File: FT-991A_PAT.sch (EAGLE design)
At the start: 24 parts, among them Q1 J310, Q2 BFS17

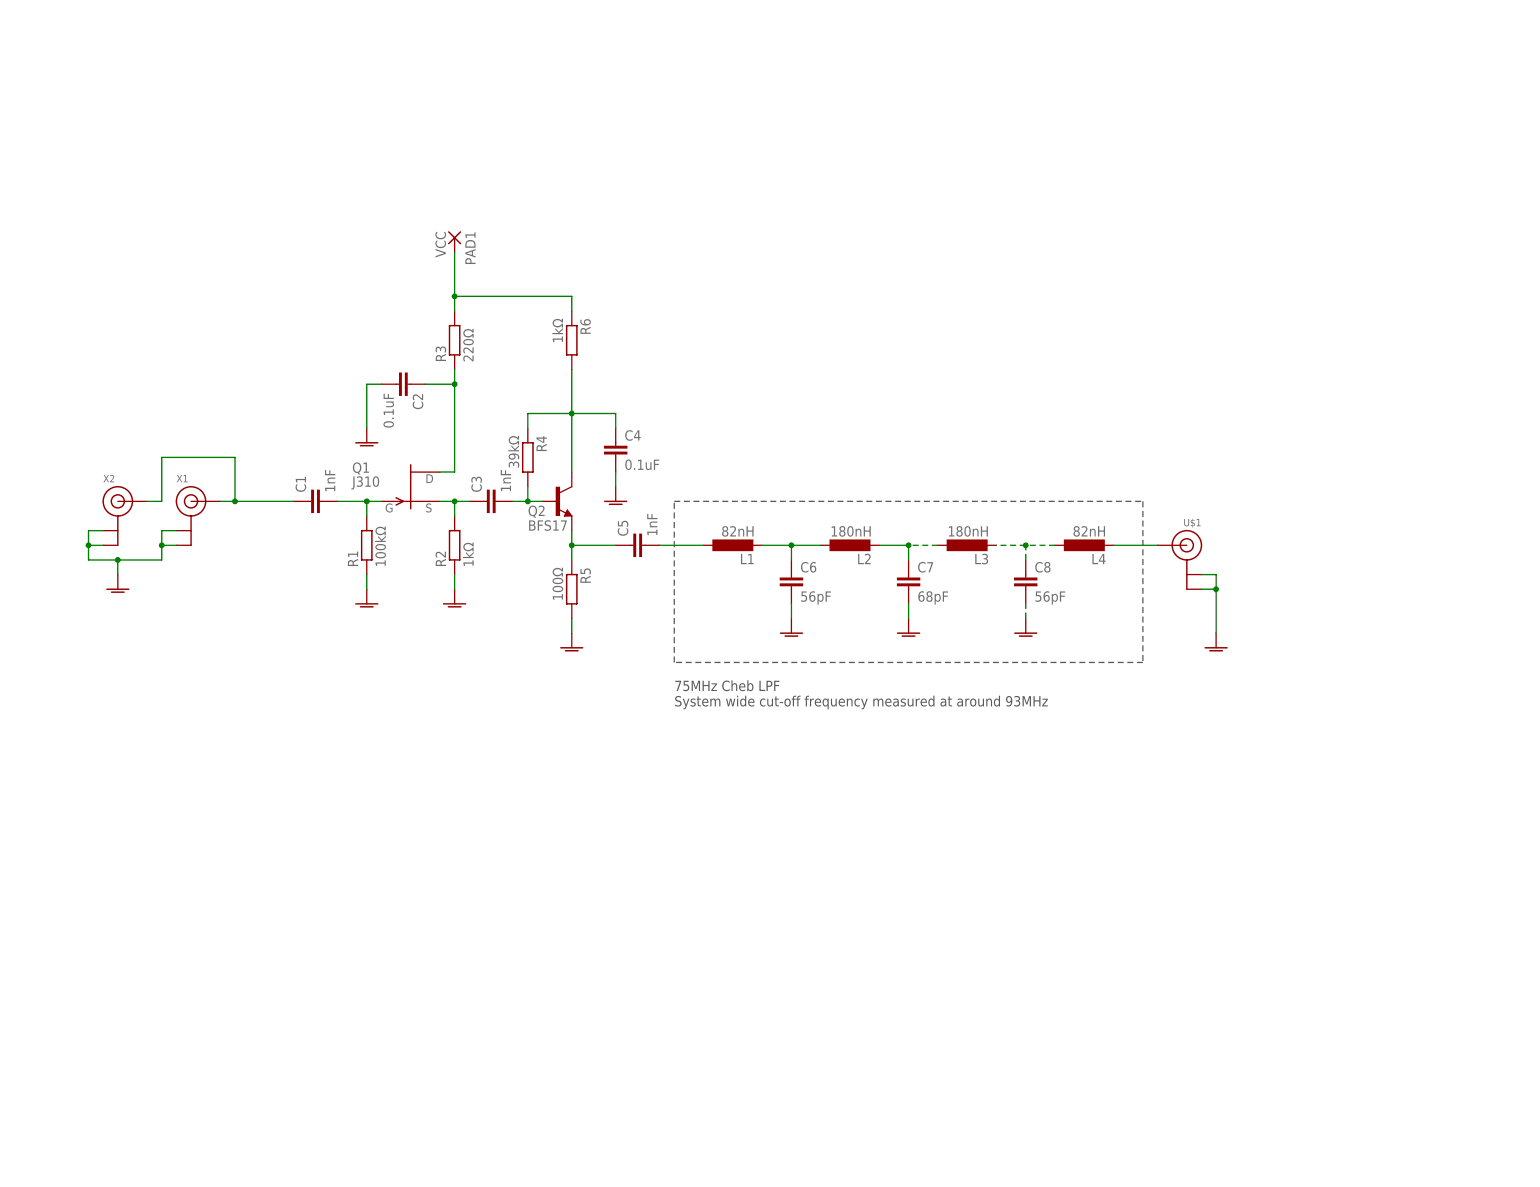
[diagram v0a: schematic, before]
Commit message: Revision D
- Reusing OE2DOR design
- Added a AND gate and a switch to be able to control the IF traffic
to the dongle
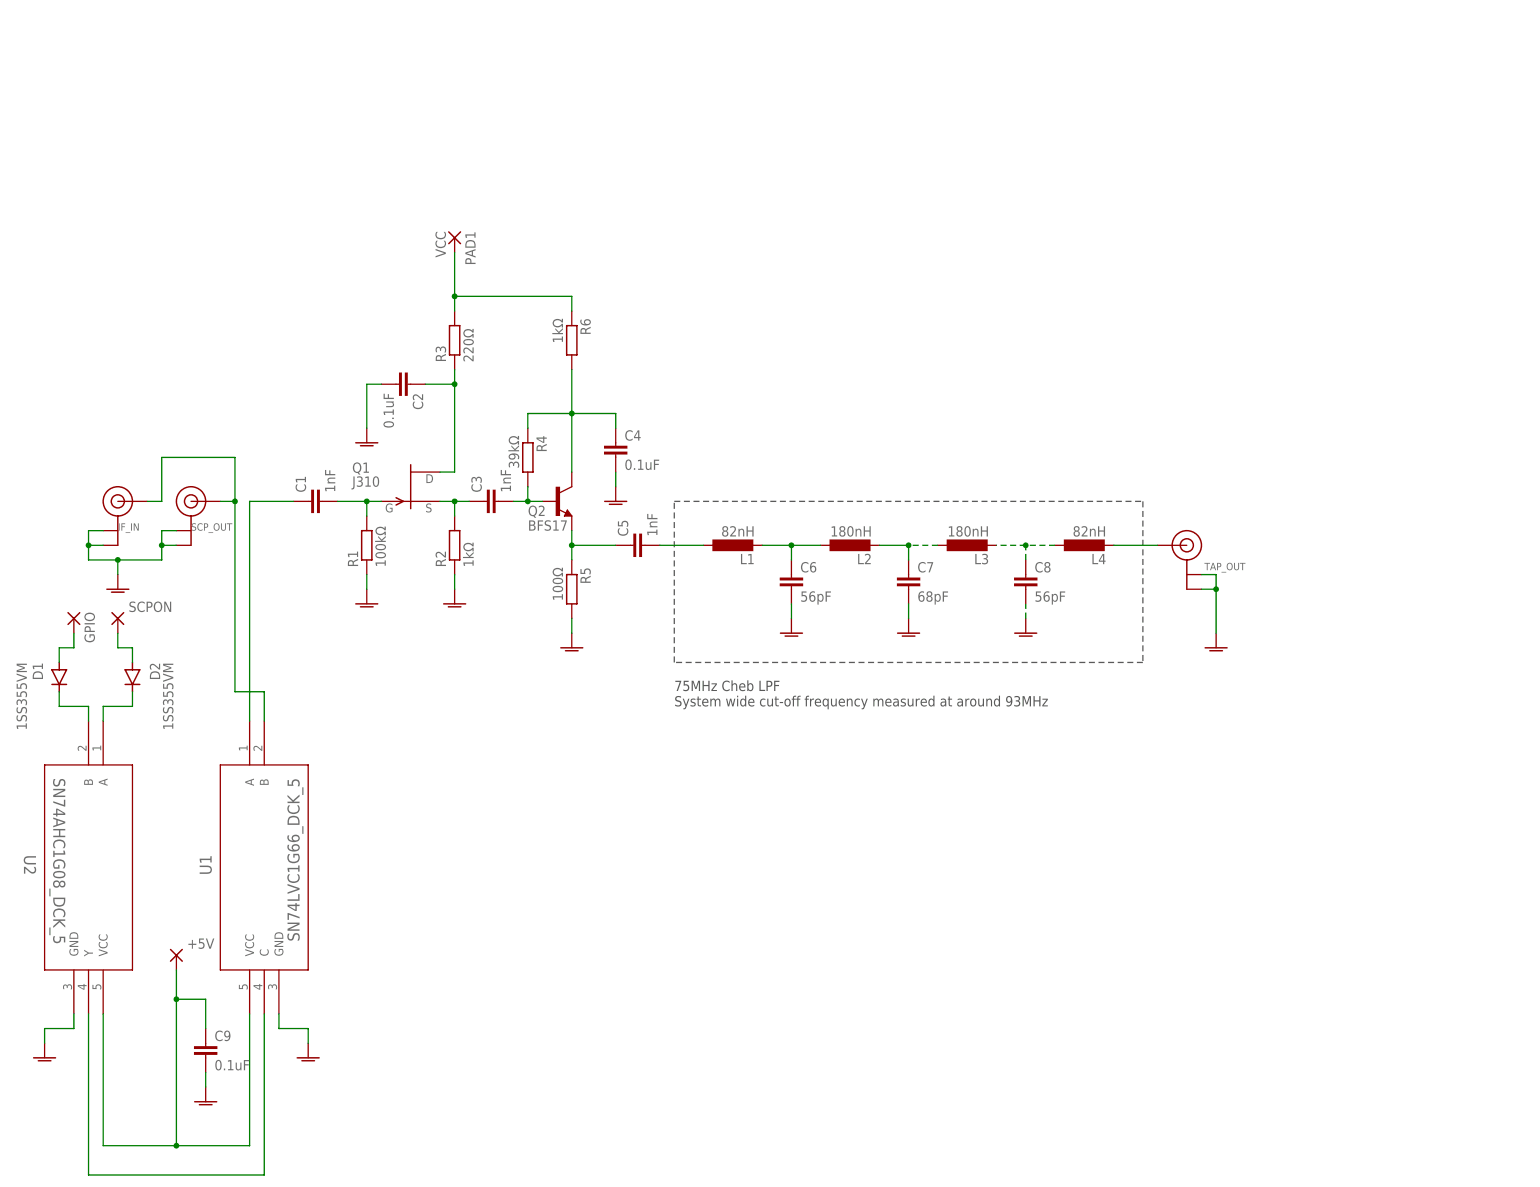
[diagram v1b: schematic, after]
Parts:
- added +5V, GPIO, SCPON: WIREPADSMD1,27-254, wirepad:WIREPADSMD1,27-254
- added C9: 0.1uF, rcl:C-EUC0805K
- added D1, D2: 1SS355VM, diode:DIODE-SOD323-W
- added U1: SN74LVC1G66_DCK_5, sn74lvc1g66-dck:SN74LVC1G66_DCK_5
- added U2: SN74AHC1G08_DCK_5, sn74ahc1g08-dck:SN74AHC1G08_DCK_5
- TAP_OUT: value (none) -> TAP_OUT
- X1: value (none) -> SCP_OUT
- X2: value (none) -> IF_IN
- renumbered U$1 to TAP_OUT
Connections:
- new net N$16: D1.A, GPIO.P
- new net N$17: D1.C, U2.B
- new net N$18: D2.A, SCPON.P
- new net N$20: D2.C, U2.A
- new net N$22: U1.C, U2.Y
- new net N$7: U1.B, X1.SIGNAL, X2.SIGNAL
- new net VCC: +5V.P, C9.1, U1.VCC, U2.VCC
- net GNDA: now also C9.2, U1.GND, U2.GND
- net N$14: now also U1.A; no longer X1.SIGNAL, X2.SIGNAL

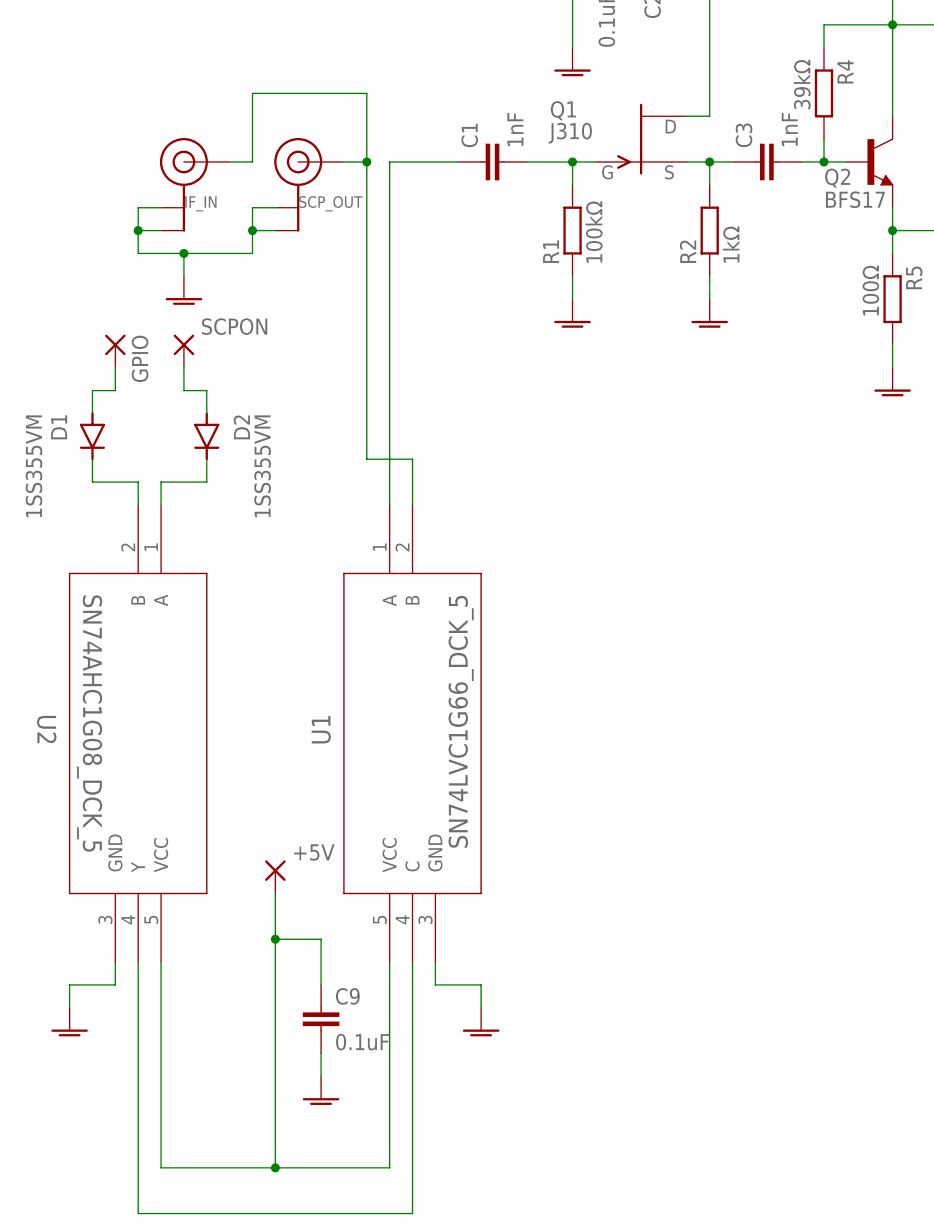
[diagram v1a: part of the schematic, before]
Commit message: Revision E
 - Now sports a RF switch (PE4259) instead of a regular Analog switch
   (was: SN74LVC1G66);
   * Also contains its resistors as per reference design;
- Changed voltage from 5V to 3.3V to Switch and AND port;
- SDR output will be grounded by default when switch is in default state
  (RF 2 port) port
- Updated list of contributors in Silk Screen.
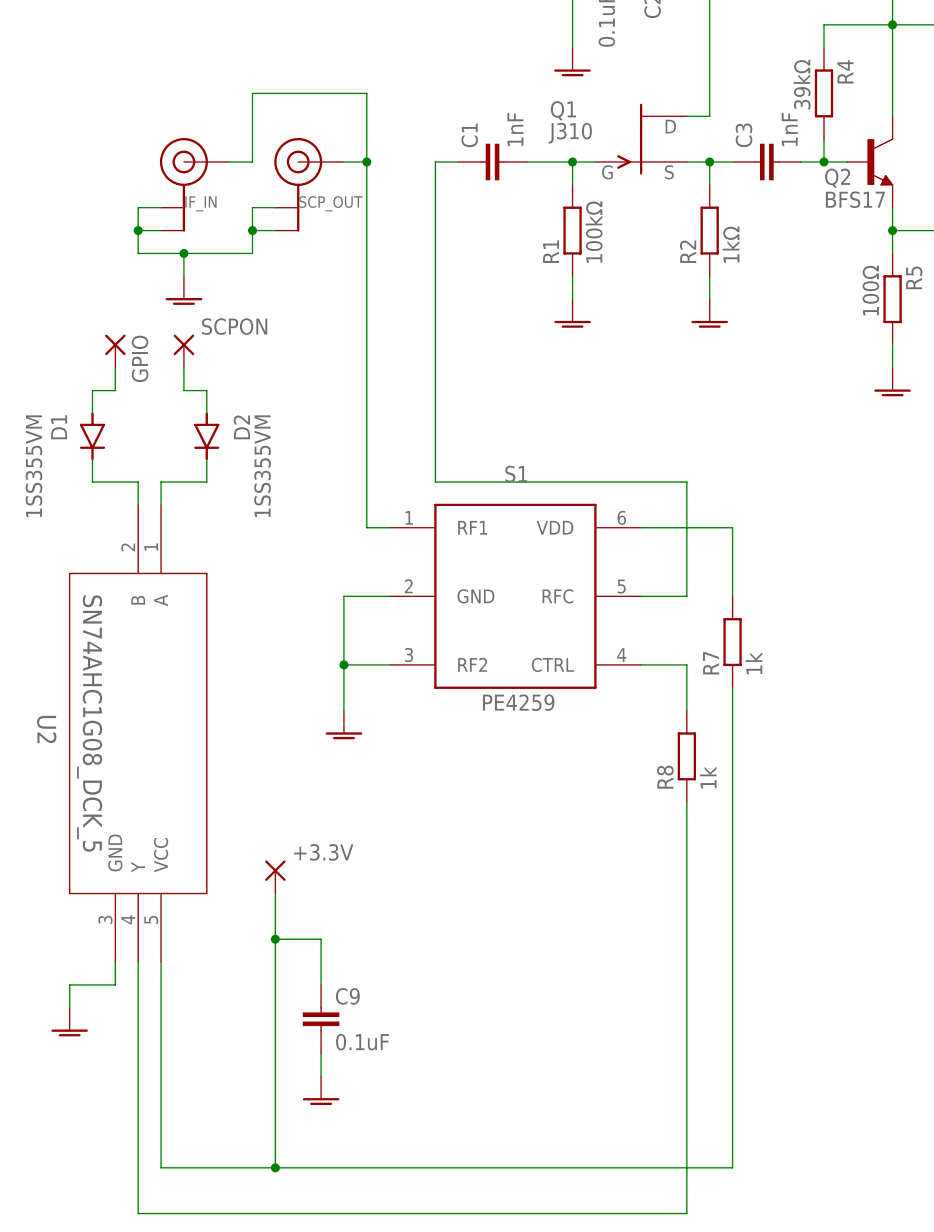
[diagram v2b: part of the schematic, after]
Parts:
- removed U1: SN74LVC1G66_DCK_5, sn74lvc1g66-dck:SN74LVC1G66_DCK_5
- added R7, R8: 1k, rcl:R-EU_R0805
- added S1: PE4259, psemi:PE4259
- renumbered +5V to +3.3V
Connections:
- removed net N$14: C1.1, U1.A
- new net N$15: C1.1, S1.RFC
- new net N$19: R8.2, S1.CTRL
- new net VDD: R7.2, S1.VDD
- net GNDA: now also S1.GND, S1.RF2; no longer U1.GND
- net N$22: now also R8.1; no longer U1.C
- net N$7: now also S1.RF1; no longer U1.B
- net VCC: now also R7.1; no longer U1.VCC
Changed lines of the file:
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@@
 <attribute name="PROJECT_INFO" value="Yaesu FT-991A Panadapter with Signal Control"/>
 <attribute name="PROJECT_NAME" value="FT-991A PAT &amp; SDR"/>
-<attribute name="REVISION_ID" value="D"/>
+<attribute name="REVISION_ID" value="E"/>
 </attributes>
 <variantdefs>
@@
 <part name="X2" library="adafruit" deviceset="ANTENNA_U.FL" device="" value="IF_IN"/>
 <part name="GND11" library="supply1" deviceset="GNDA" device=""/>
-<part name="U1" library="sn74lvc1g66-dck" deviceset="SN74LVC1G66_DCK_5" device=""/>
 <part name="U2" library="sn74ahc1g08-dck" deviceset="SN74AHC1G08_DCK_5" device=""/>
 <part name="D1" library="diode" library_urn="urn:adsk.eagle:library:210" deviceset="DIODE-" device="SOD323-W" package3d_urn="urn:adsk.eagle:package:43418/1" value="1SS355VM"/>
@@
 <part name="GPIO" library="wirepad" library_urn="urn:adsk.eagle:library:412" deviceset="WIREPAD" device="SMD1,27-254" package3d_urn="urn:adsk.eagle:package:30839/1" value=""/>
 <part name="SCPON" library="wirepad" library_urn="urn:adsk.eagle:library:412" deviceset="WIREPAD" device="SMD1,27-254" package3d_urn="urn:adsk.eagle:package:30839/1" value=""/>
-<part name="+5V" library="wirepad" library_urn="urn:adsk.eagle:library:412" deviceset="WIREPAD" device="SMD1,27-254" package3d_urn="urn:adsk.eagle:package:30839/1" value=""/>
+<part name="+3.3V" library="wirepad" library_urn="urn:adsk.eagle:library:412" deviceset="WIREPAD" device="SMD1,27-254" package3d_urn="urn:adsk.eagle:package:30839/1" value=""/>
+<part name="S1" library="psemi" deviceset="PE4259" device="" value="PE4259"/>
+<part name="R7" library="rcl" deviceset="R-EU_" device="R0805" value="1k"/>
+<part name="R8" library="rcl" deviceset="R-EU_" device="R0805" value="1k"/>
 </parts>
 <sheets>
@@
 </instance>
 <instance part="GND11" gate="1" x="78.74" y="114.3" smashed="yes"/>
-<instance part="U1" gate="A" x="101.6" y="91.44" smashed="yes" rot="MR270">
-<attribute name="NAME" x="95.0214" y="68.2244" size="2.0828" layer="95" ratio="6" rot="SMR270"/>
-<attribute name="VALUE" x="110.2614" y="81.5594" size="2.0828" layer="96" ratio="6" rot="SMR270"/>
-</instance>
 <instance part="U2" gate="A" x="76.2" y="91.44" smashed="yes" rot="R270">
 <attribute name="NAME" x="62.4586" y="68.2244" size="2.0828" layer="95" ratio="6" rot="SR270"/>
@@
 </instance>
 <instance part="GND10" gate="1" x="66.04" y="33.02" smashed="yes"/>
-<instance part="GND12" gate="1" x="111.76" y="33.02" smashed="yes"/>
+<instance part="GND12" gate="1" x="96.52" y="66.04" smashed="yes"/>
 <instance part="GPIO" gate="G$1" x="71.12" y="109.22" smashed="yes" rot="R270">
 <attribute name="NAME" x="72.9742" y="110.363" size="1.778" layer="95" rot="R270"/>
@@
 <attribute name="VALUE" x="80.518" y="107.823" size="1.778" layer="96"/>
 </instance>
-<instance part="+5V" gate="G$1" x="88.9" y="50.8" smashed="yes" rot="R270">
+<instance part="+3.3V" gate="G$1" x="88.9" y="50.8" smashed="yes" rot="R270">
 <attribute name="NAME" x="90.7542" y="51.943" size="1.778" layer="95"/>
 <attribute name="VALUE" x="90.678" y="49.403" size="1.778" layer="96"/>
+</instance>
+<instance part="S1" gate="G$1" x="114.3" y="81.28" smashed="yes">
+<attribute name="NAME" x="114.3" y="93.98" size="1.778" layer="95" font="vector"/>
+<attribute name="VALUE" x="111.76" y="68.58" size="1.778" layer="96" font="vector"/>
+</instance>
+<instance part="R7" gate="G$1" x="139.7" y="76.2" smashed="yes" rot="R90">
+<attribute name="NAME" x="138.2014" y="72.39" size="1.778" layer="95" rot="R90"/>
+<attribute name="VALUE" x="143.002" y="72.39" size="1.778" layer="96" rot="R90"/>
+</instance>
+<instance part="R8" gate="G$1" x="134.62" y="63.5" smashed="yes" rot="R90">
+<attribute name="NAME" x="133.1214" y="59.69" size="1.778" layer="95" rot="R90"/>
+<attribute name="VALUE" x="137.922" y="59.69" size="1.778" layer="96" rot="R90"/>
 </instance>
 </instances>
@@
 </segment>
 <segment>
-<pinref part="U1" gate="A" pin="GND"/>
-<wire x1="106.68" y1="40.64" x2="106.68" y2="38.1" width="0.1524" layer="91"/>
-<wire x1="106.68" y1="38.1" x2="111.76" y2="38.1" width="0.1524" layer="91"/>
-<wire x1="111.76" y1="38.1" x2="111.76" y2="35.56" width="0.1524" layer="91"/>
+<pinref part="S1" gate="G$1" pin="GND"/>
 <pinref part="GND12" gate="1" pin="GNDA"/>
+<wire x1="101.6" y1="81.28" x2="96.52" y2="81.28" width="0.1524" layer="91"/>
+<wire x1="96.52" y1="81.28" x2="96.52" y2="73.66" width="0.1524" layer="91"/>
+<pinref part="S1" gate="G$1" pin="RF2"/>
+<wire x1="96.52" y1="73.66" x2="96.52" y2="68.58" width="0.1524" layer="91"/>
+<wire x1="101.6" y1="73.66" x2="96.52" y2="73.66" width="0.1524" layer="91"/>
+<junction x="96.52" y="73.66"/>
 </segment>
 </net>
@@
 <wire x1="76.2" y1="40.64" x2="76.2" y2="17.78" width="0.1524" layer="91"/>
 <wire x1="76.2" y1="17.78" x2="88.9" y2="17.78" width="0.1524" layer="91"/>
-<pinref part="U1" gate="A" pin="VCC"/>
-<wire x1="88.9" y1="17.78" x2="101.6" y2="17.78" width="0.1524" layer="91"/>
-<wire x1="101.6" y1="17.78" x2="101.6" y2="40.64" width="0.1524" layer="91"/>
 <junction x="88.9" y="17.78"/>
 <wire x1="88.9" y1="48.26" x2="88.9" y2="43.18" width="0.1524" layer="91"/>
@@
 <pinref part="C9" gate="G$1" pin="1"/>
 <wire x1="93.98" y1="43.18" x2="93.98" y2="38.1" width="0.1524" layer="91"/>
-<pinref part="+5V" gate="G$1" pin="P"/>
+<pinref part="+3.3V" gate="G$1" pin="P"/>
 <wire x1="88.9" y1="17.78" x2="88.9" y2="43.18" width="0.1524" layer="91"/>
 <junction x="88.9" y="43.18"/>
+<wire x1="88.9" y1="17.78" x2="139.7" y2="17.78" width="0.1524" layer="91"/>
+<wire x1="139.7" y1="17.78" x2="139.7" y2="71.12" width="0.1524" layer="91"/>
+<pinref part="R7" gate="G$1" pin="1"/>
 </segment>
 </net>
@@
 <pinref part="U2" gate="A" pin="Y"/>
 <wire x1="73.66" y1="40.64" x2="73.66" y2="12.7" width="0.1524" layer="91"/>
-<wire x1="73.66" y1="12.7" x2="104.14" y2="12.7" width="0.1524" layer="91"/>
-<pinref part="U1" gate="A" pin="C"/>
-<wire x1="104.14" y1="12.7" x2="104.14" y2="40.64" width="0.1524" layer="91"/>
+<wire x1="73.66" y1="12.7" x2="134.62" y2="12.7" width="0.1524" layer="91"/>
+<wire x1="134.62" y1="12.7" x2="134.62" y2="58.42" width="0.1524" layer="91"/>
+<pinref part="R8" gate="G$1" pin="1"/>
 </segment>
 </net>
@@
 <net name="N$7" class="0">
 <segment>
-<pinref part="X1" gate="G$1" pin="SIGNAL"/>
-<wire x1="99.06" y1="129.54" x2="96.52" y2="129.54" width="0.1524" layer="91"/>
-<wire x1="99.06" y1="137.16" x2="99.06" y2="129.54" width="0.1524" layer="91"/>
 <wire x1="86.36" y1="137.16" x2="99.06" y2="137.16" width="0.1524" layer="91"/>
 <wire x1="86.36" y1="129.54" x2="86.36" y2="137.16" width="0.1524" layer="91"/>
 <pinref part="X2" gate="G$1" pin="SIGNAL"/>
 <wire x1="83.82" y1="129.54" x2="86.36" y2="129.54" width="0.1524" layer="91"/>
-<wire x1="99.06" y1="129.54" x2="99.06" y2="96.52" width="0.1524" layer="91"/>
+<pinref part="S1" gate="G$1" pin="RF1"/>
+<wire x1="99.06" y1="137.16" x2="99.06" y2="129.54" width="0.1524" layer="91"/>
+<wire x1="99.06" y1="129.54" x2="99.06" y2="88.9" width="0.1524" layer="91"/>
+<wire x1="99.06" y1="88.9" x2="101.6" y2="88.9" width="0.1524" layer="91"/>
+<pinref part="X1" gate="G$1" pin="SIGNAL"/>
+<wire x1="96.52" y1="129.54" x2="99.06" y2="129.54" width="0.1524" layer="91"/>
 <junction x="99.06" y="129.54"/>
-<wire x1="99.06" y1="96.52" x2="104.14" y2="96.52" width="0.1524" layer="91"/>
-<pinref part="U1" gate="A" pin="B"/>
-<wire x1="104.14" y1="96.52" x2="104.14" y2="91.44" width="0.1524" layer="91"/>
-</segment>
-</net>
-<net name="N$14" class="0">
-<segment>
-<pinref part="U1" gate="A" pin="A"/>
-<wire x1="101.6" y1="91.44" x2="101.6" y2="129.54" width="0.1524" layer="91"/>
+</segment>
+</net>
+<net name="N$15" class="0">
+<segment>
 <pinref part="C1" gate="G$1" pin="1"/>
-<wire x1="101.6" y1="129.54" x2="109.22" y2="129.54" width="0.1524" layer="91"/>
+<wire x1="106.68" y1="129.54" x2="109.22" y2="129.54" width="0.1524" layer="91"/>
+<wire x1="106.68" y1="129.54" x2="106.68" y2="93.98" width="0.1524" layer="91"/>
+<wire x1="106.68" y1="93.98" x2="134.62" y2="93.98" width="0.1524" layer="91"/>
+<pinref part="S1" gate="G$1" pin="RFC"/>
+<wire x1="134.62" y1="93.98" x2="134.62" y2="81.28" width="0.1524" layer="91"/>
+<wire x1="134.62" y1="81.28" x2="129.54" y2="81.28" width="0.1524" layer="91"/>
+</segment>
+</net>
+<net name="VDD" class="0">
+<segment>
+<pinref part="S1" gate="G$1" pin="VDD"/>
+<wire x1="139.7" y1="88.9" x2="129.54" y2="88.9" width="0.1524" layer="91"/>
+<wire x1="139.7" y1="81.28" x2="139.7" y2="88.9" width="0.1524" layer="91"/>
+<pinref part="R7" gate="G$1" pin="2"/>
+</segment>
+</net>
+<net name="N$19" class="0">
+<segment>
+<pinref part="S1" gate="G$1" pin="CTRL"/>
+<wire x1="134.62" y1="73.66" x2="129.54" y2="73.66" width="0.1524" layer="91"/>
+<wire x1="134.62" y1="68.58" x2="134.62" y2="73.66" width="0.1524" layer="91"/>
+<pinref part="R8" gate="G$1" pin="2"/>
 </segment>
 </net>
@@
 </sheet>
 </sheets>
+<errors>
+</errors>
 </schematic>
 </drawing>
